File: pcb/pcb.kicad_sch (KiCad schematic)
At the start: 143 parts, among them J1 USB_C_Receptacle_USB2.0_14P, J2 Conn_01x06_Socket, M1 Ezurio BL54L15 (nrf54L15) mod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, SW1 SW_DIP_x01

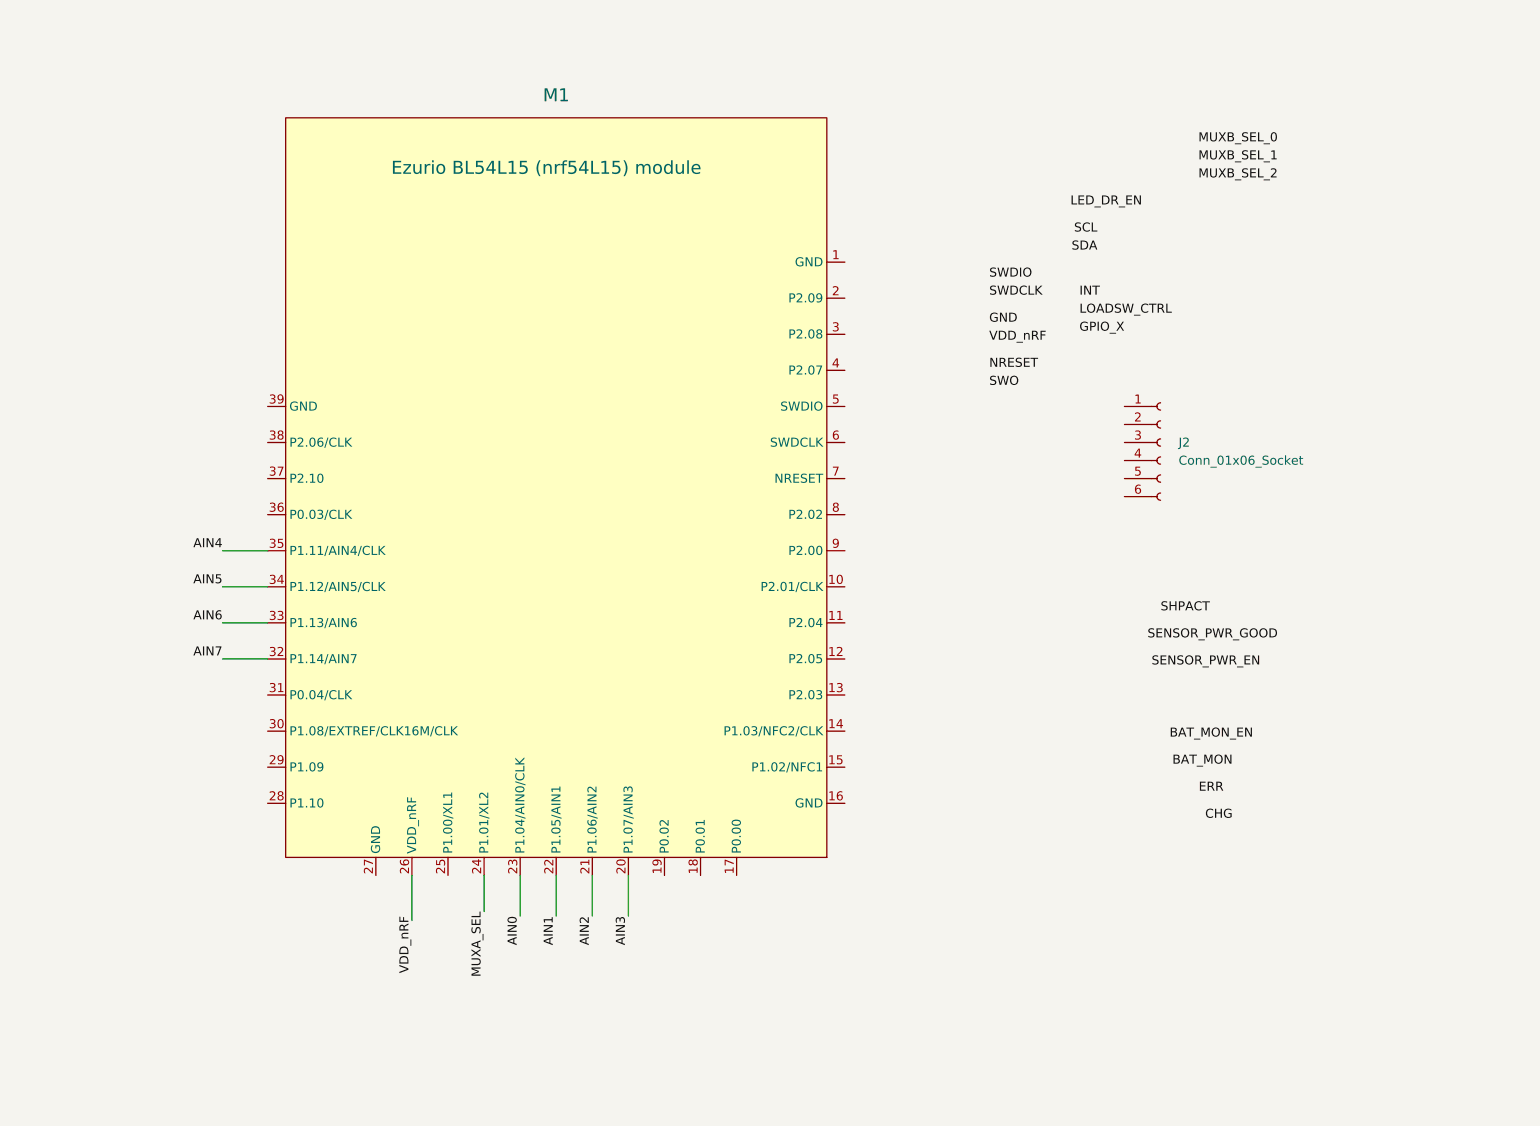
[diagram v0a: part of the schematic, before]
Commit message: M  pcb/pcb.kicad_pcb M  pcb/pcb.kicad_prl M  pcb/pcb.kicad_pro M  pcb/pcb.kicad_sch M  placefp.py A  tmr-footprints/SAMTEC-CLP-105-02-X-D-A-altium.kicad_mod A  tmr-footprints/SAMTEC-CLP-105-02-X-D-A.kicad_mod
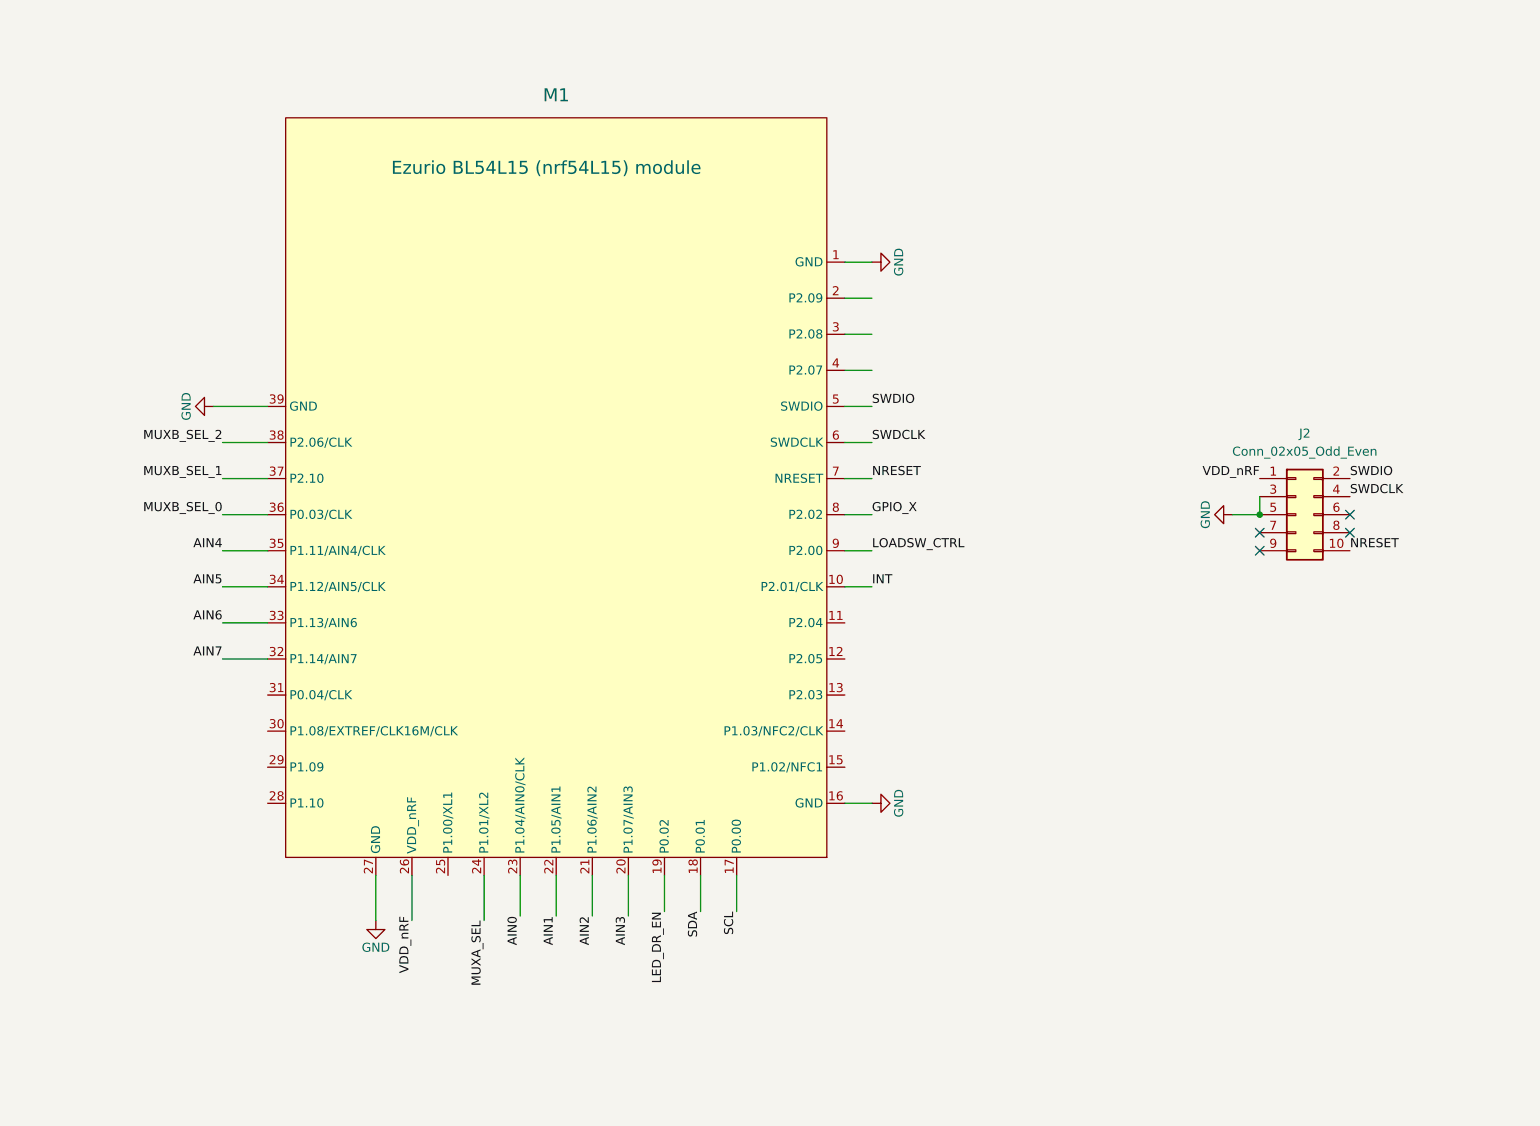
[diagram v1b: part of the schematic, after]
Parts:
- removed J2: Conn_01x06_Socket, symbol Connector:Conn_01x06_Socket
- added J2: Conn_02x05_Odd_Even, tmr-lib:SAMTEC-CLP-105-02-X-D-A, symbol Connector_Generic:Conn_02x05_Odd_Even
- SW1: footprint (none) -> Button_Switch_SMD:SW_SPST_Omron_B3FS-105xP
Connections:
- net GND: now also M1.1 (GND), M1.16 (GND), M1.27 (GND), M1.39 (GND), J2.3 (Pin_3), J2.5 (Pin_5)
- net GPIO_X: now also M1.8 (P2.02)
- net INT: now also M1.10 (P2.01/CLK)
- net LED_DR_EN: now also M1.19 (P0.02)
- net LOADSW_CTRL: now also M1.9 (P2.00)
- net MUXB_SEL_0: now also M1.36 (P0.03/CLK)
- net MUXB_SEL_1: now also M1.37 (P2.10)
- net MUXB_SEL_2: now also M1.38 (P2.06/CLK)
- net NRESET: now also M1.7 (NRESET), J2.10 (Pin_10)
- net SCL: now also M1.17 (P0.00)
- net SDA: now also M1.18 (P0.01)
- net SWDCLK: now also M1.6 (SWDCLK), J2.4 (Pin_4)
- net SWDIO: now also M1.5 (SWDIO), J2.2 (Pin_2)
- net VDDIO: now also J2.1 (Pin_1)
- no-connect marks 9 -> 13

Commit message: M  pcb/pcb.kicad_pcb M  pcb/pcb.kicad_prl M  pcb/pcb.kicad_sch M  placefp.py M  tmr-footprints/Ezurio_BL54L15_Module.kicad_mod
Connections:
- net CS0: now also D24.1 (K), D38.1 (K), D53.1 (K), D9.1 (K); no longer D1.1 (K), D16.1 (K), D30.1 (K), D45.1 (K)
- net CS1: now also D10.1 (K), D25.1 (K), D39.1 (K), D54.1 (K); no longer D17.1 (K), D2.1 (K), D31.1 (K), D46.1 (K)
- net CS10: now also D1.1 (K), D16.1 (K), D30.1 (K), D45.1 (K); no longer D24.1 (K), D38.1 (K), D53.1 (K), D9.1 (K)
- net CS11: now also D17.1 (K), D2.1 (K), D31.1 (K), D46.1 (K); no longer D10.1 (K), D25.1 (K), D39.1 (K), D54.1 (K)
- net CS12: now also D18.1 (K), D3.1 (K), D32.1 (K), D47.1 (K); no longer D11.1 (K), D26.1 (K), D40.1 (K), D55.1 (K)
- net CS13: now also D19.1 (K), D33.1 (K), D4.1 (K), D48.1 (K); no longer D12.1 (K), D27.1 (K), D41.1 (K), D56.1 (K)
- net CS14: now also D20.1 (K), D34.1 (K), D49.1 (K), D5.1 (K); no longer D13.1 (K), D28.1 (K), D42.1 (K), D57.1 (K)
- net CS15: now also D21.1 (K), D35.1 (K), D50.1 (K), D6.1 (K); no longer D14.1 (K), D29.1 (K), D43.1 (K), D58.1 (K)
- net CS16: now also D22.1 (K), D36.1 (K), D51.1 (K), D7.1 (K); no longer D15.1 (K), D44.1 (K), D71.1 (K), D72.1 (K)
- net CS17: now also D23.1 (K), D37.1 (K), D52.1 (K), D8.1 (K); no longer D67.1 (K), D68.1 (K), D69.1 (K), D70.1 (K)
- net CS2: now also D11.1 (K), D26.1 (K), D40.1 (K), D55.1 (K); no longer D18.1 (K), D3.1 (K), D32.1 (K), D47.1 (K)
- net CS3: now also D12.1 (K), D27.1 (K), D41.1 (K), D56.1 (K); no longer D19.1 (K), D33.1 (K), D4.1 (K), D48.1 (K)
- net CS4: now also D13.1 (K), D28.1 (K), D42.1 (K), D57.1 (K); no longer D20.1 (K), D34.1 (K), D49.1 (K), D5.1 (K)
- net CS5: now also D14.1 (K), D29.1 (K), D43.1 (K), D58.1 (K); no longer D21.1 (K), D35.1 (K), D50.1 (K), D6.1 (K)
- net CS6: now also D15.1 (K), D44.1 (K), D71.1 (K), D72.1 (K); no longer D22.1 (K), D36.1 (K), D51.1 (K), D7.1 (K)
- net CS7: now also D67.1 (K), D68.1 (K), D69.1 (K), D70.1 (K); no longer D23.1 (K), D37.1 (K), D52.1 (K), D8.1 (K)
- net CS8: now also D63.1 (K), D64.1 (K), D65.1 (K), D66.1 (K); no longer D59.1 (K), D60.1 (K), D61.1 (K), D62.1 (K)
- net CS9: now also D59.1 (K), D60.1 (K), D61.1 (K), D62.1 (K); no longer D63.1 (K), D64.1 (K), D65.1 (K), D66.1 (K)
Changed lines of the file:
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@@
 	)
 	(label "CS2"
-		(at 396.24 426.72 180)
+		(at 467.36 426.72 180)
 		(effects
 			(font
@@
 	)
 	(label "CS3"
-		(at 405.13 426.72 180)
+		(at 476.25 426.72 180)
 		(effects
 			(font
@@
 	)
 	(label "CS16"
-		(at 502.92 426.72 180)
+		(at 431.8 426.72 180)
 		(effects
 			(font
@@
 		)
 	)
-	(label "CS9"
-		(at 414.02 441.96 180)
-		(effects
-			(font
-				(size 1.27 1.27)
-			)
-			(justify right bottom)
-		)
-	)
 	(label "ANA_70"
 		(at 170.18 294.64 180)
@@
 	)
 	(label "CS1"
-		(at 387.35 426.72 180)
+		(at 458.47 426.72 180)
 		(effects
 			(font
@@
 	)
 	(label "CS6"
-		(at 431.8 426.72 180)
+		(at 502.92 426.72 180)
 		(effects
 			(font
@@
 	)
 	(label "CS12"
-		(at 467.36 426.72 180)
+		(at 396.24 426.72 180)
 		(effects
 			(font
@@
 		)
 	)
+	(label "CS9"
+		(at 378.46 441.96 180)
+		(effects
+			(font
+				(size 1.27 1.27)
+			)
+			(justify right bottom)
+		)
+	)
 	(label "ANA_34"
 		(at 170.18 223.52 180)
@@
 	)
 	(label "CS7"
-		(at 440.69 426.72 180)
+		(at 476.25 441.96 180)
 		(effects
 			(font
@@
 	)
 	(label "CS5"
-		(at 422.91 426.72 180)
+		(at 494.03 426.72 180)
 		(effects
 			(font
@@
 	)
 	(label "CS10"
-		(at 449.58 426.72 180)
+		(at 378.46 426.72 180)
 		(effects
 			(font
@@
 	)
 	(label "CS15"
-		(at 494.03 426.72 180)
+		(at 422.91 426.72 180)
 		(effects
 			(font
@@
 		)
 	)
-	(label "CS17"
-		(at 476.25 441.96 180)
-		(effects
-			(font
-				(size 1.27 1.27)
-			)
-			(justify right bottom)
-		)
-	)
 	(label "ANA_71"
 		(at 204.47 134.62 0)
@@
 		)
 	)
-	(label "CS16"
+	(label "CS6"
 		(at 494.03 441.96 180)
 		(effects
@@
 		)
 	)
-	(label "CS16"
+	(label "CS6"
 		(at 485.14 441.96 180)
 		(effects
@@
 	)
 	(label "CS11"
-		(at 458.47 426.72 180)
+		(at 387.35 426.72 180)
 		(effects
 			(font
@@
 	)
 	(label "CS4"
-		(at 414.02 426.72 180)
+		(at 485.14 426.72 180)
 		(effects
 			(font
@@
 	)
 	(label "CS8"
-		(at 378.46 441.96 180)
+		(at 414.02 441.96 180)
 		(effects
 			(font
@@
 		)
 	)
+	(label "CS17"
+		(at 440.69 426.72 180)
+		(effects
+			(font
+				(size 1.27 1.27)
+			)
+			(justify right bottom)
+		)
+	)
 	(label "ANA_52"
 		(at 213.36 279.4 180)
@@
 	)
 	(label "CS14"
-		(at 485.14 426.72 180)
+		(at 414.02 426.72 180)
 		(effects
 			(font
@@
 	)
 	(label "CS0"
-		(at 378.46 426.72 180)
+		(at 449.58 426.72 180)
 		(effects
 			(font
@@
 	)
 	(label "CS13"
-		(at 476.25 426.72 180)
-		(effects
-			(font
+		(at 405.13 426.72 180)
+		(effects
+			(font

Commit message: M  pcb/pcb.kicad_pcb M  pcb/pcb.kicad_prl M  pcb/pcb.kicad_sch M  pcb/switch.kicad_sch M  placefp.py A  tmr-footprints/Button_Switch_3x4x2.5.kicad_mod A  tmr-footprints/Panasonic_EVPAE.kicad_mod
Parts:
- removed J1: USB_C_Receptacle_USB2.0_14P, symbol Connector:USB_C_Receptacle_USB2.0_14P
- removed JLC1: JLC_Order_Num, tmr-lib:JLC_Order_Num, symbol giri:JLC_Order_Num
- added JLC1: JLC_Order_Num, tmr-lib:JLC_Order_Num, symbol tmr-lib:JLC_Order_Num
- added JTAG2: Conn_02x05_Odd_Even, Connector:Tag-Connect_TC2050-IDC-FP_2x05_P1.27mm_Vertical, symbol Connector_Generic:Conn_02x05_Odd_Even
- BAT1: value Battery_Pack_PS5 -> ~; footprint Connector_JST:JST_EH_S3B-EH_1x03_P2.50mm_Horizontal -> Connector_JST:JST_SH_BM03B-SRSS-TB_1x03-1MP_P1.00mm_Vertical
- SW1: footprint Button_Switch_SMD:SW_SPST_Omron_B3FS-105xP -> tmr-lib:Button_Switch_3x4x2.5
- renumbered C6 to C1, C15 to C10, C16 to C11, C17 to C12, C18 to C13, C5 to C14, C7 to C15, C20 to C16, C21 to C17, C22 to C18, C23 to C19, C8 to C2, C24 to C20, C12 to C21, C13 to C22, C14 to C23, C27 to C24, C28 to C25, C29 to C26, C30 to C27, C19 to C28, C25 to C29, C9 to C3, C26 to C30, C10 to C4, C11 to C5, C1 to C6, C2 to C7, C3 to C8, C4 to C9, J2 to JTAG1
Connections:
- net VCC_tmr is gone; now on net VCCS: C23.1, PMIC1.29 (LSOUT1/VOUTLDO1)
- net GND: now also JTAG2.3 (Pin_3), JTAG2.5 (Pin_5)
- net NRESET: now also JTAG2.10 (Pin_10)
- net SWDCLK: now also JTAG2.4 (Pin_4)
- net SWDIO: now also JTAG2.2 (Pin_2)
- net VCCS: no longer C22.1, L2.1, PMIC1.28 (LSIN1/VINLDO1), PMIC1.32 (VOUT2)
- net VDDIO: now also JTAG2.1 (Pin_1)
- new net VOUT2: C22.1, L2.1, PMIC1.28 (LSIN1/VINLDO1), PMIC1.32 (VOUT2)
- no-connect marks 13 -> 26
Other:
- moved on the sheet: BAT1, C14, C15, C21, C22, C23, C28, C29, C30, C31, C32, C6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

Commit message: M  pcb/pcb.kicad_pcb M  pcb/pcb.kicad_sch A  tmr-footprints/MountingHole_2.2mm_M2_ISO7380_Pad_TopBottom.kicad_mod
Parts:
- Hs1, Hs10, Hs11, Hs12, Hs2, Hs3, Hs4, Hs5, Hs6, Hs7, Hs8, Hs9: footprint MountingHole:MountingHole_2.2mm_M2_ISO7380_Pad_TopBottom -> tmr-lib:MountingHole_2.2mm_M2_ISO7380_Pad_TopBottom
- JTAG2: footprint Connector:Tag-Connect_TC2050-IDC-FP_2x05_P1.27mm_Vertical -> Connector:Tag-Connect_TC2050-IDC-NL_2x05_P1.27mm_Vertical
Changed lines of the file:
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@@
 			)
 		)
-		(property "Footprint" "MountingHole:MountingHole_2.2mm_M2_ISO7380_Pad_TopBottom"
+		(property "Footprint" "tmr-lib:MountingHole_2.2mm_M2_ISO7380_Pad_TopBottom"
 			(at 359.41 364.49 0)
 			(effects
@@
 			)
 		)
-		(property "Footprint" "MountingHole:MountingHole_2.2mm_M2_ISO7380_Pad_TopBottom"
+		(property "Footprint" "tmr-lib:MountingHole_2.2mm_M2_ISO7380_Pad_TopBottom"
 			(at 359.41 372.11 0)
 			(effects
@@
 			)
 		)
-		(property "Footprint" "Connector:Tag-Connect_TC2050-IDC-FP_2x05_P1.27mm_Vertical"
+		(property "Footprint" "Connector:Tag-Connect_TC2050-IDC-NL_2x05_P1.27mm_Vertical"
 			(at 492.76 133.35 0)
 			(effects
@@
 			)
 		)
-		(property "Footprint" "MountingHole:MountingHole_2.2mm_M2_ISO7380_Pad_TopBottom"
+		(property "Footprint" "tmr-lib:MountingHole_2.2mm_M2_ISO7380_Pad_TopBottom"
 			(at 384.81 364.49 0)
 			(effects
@@
 			)
 		)
-		(property "Footprint" "MountingHole:MountingHole_2.2mm_M2_ISO7380_Pad_TopBottom"
+		(property "Footprint" "tmr-lib:MountingHole_2.2mm_M2_ISO7380_Pad_TopBottom"
 			(at 372.11 364.49 0)
 			(effects
@@
 			)
 		)
-		(property "Footprint" "MountingHole:MountingHole_2.2mm_M2_ISO7380_Pad_TopBottom"
+		(property "Footprint" "tmr-lib:MountingHole_2.2mm_M2_ISO7380_Pad_TopBottom"
 			(at 397.51 372.11 0)
 			(effects
@@
 			)
 		)
-		(property "Footprint" "MountingHole:MountingHole_2.2mm_M2_ISO7380_Pad_TopBottom"
+		(property "Footprint" "tmr-lib:MountingHole_2.2mm_M2_ISO7380_Pad_TopBottom"
 			(at 372.11 372.11 0)
 			(effects
@@
 			)
 		)
-		(property "Footprint" "MountingHole:MountingHole_2.2mm_M2_ISO7380_Pad_TopBottom"
+		(property "Footprint" "tmr-lib:MountingHole_2.2mm_M2_ISO7380_Pad_TopBottom"
 			(at 359.41 379.73 0)
 			(effects
@@
 			)
 		)
-		(property "Footprint" "MountingHole:MountingHole_2.2mm_M2_ISO7380_Pad_TopBottom"
+		(property "Footprint" "tmr-lib:MountingHole_2.2mm_M2_ISO7380_Pad_TopBottom"
 			(at 397.51 379.73 0)
 			(effects
@@
 			)
 		)
-		(property "Footprint" "MountingHole:MountingHole_2.2mm_M2_ISO7380_Pad_TopBottom"
+		(property "Footprint" "tmr-lib:MountingHole_2.2mm_M2_ISO7380_Pad_TopBottom"
 			(at 384.81 372.11 0)
 			(effects
@@
 			)
 		)
-		(property "Footprint" "MountingHole:MountingHole_2.2mm_M2_ISO7380_Pad_TopBottom"
+		(property "Footprint" "tmr-lib:MountingHole_2.2mm_M2_ISO7380_Pad_TopBottom"
 			(at 372.11 379.73 0)
 			(effects
@@
 			)
 		)
-		(property "Footprint" "MountingHole:MountingHole_2.2mm_M2_ISO7380_Pad_TopBottom"
+		(property "Footprint" "tmr-lib:MountingHole_2.2mm_M2_ISO7380_Pad_TopBottom"
 			(at 384.81 379.73 0)
 			(effects
@@
 			)
 		)
-		(property "Footprint" "MountingHole:MountingHole_2.2mm_M2_ISO7380_Pad_TopBottom"
+		(property "Footprint" "tmr-lib:MountingHole_2.2mm_M2_ISO7380_Pad_TopBottom"
 			(at 397.51 364.49 0)
 			(effects

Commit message: M  pcb/pcb.kicad_pcb M  pcb/pcb.kicad_prl M  pcb/pcb.kicad_pro M  pcb/pcb.kicad_sch M  placefp.py M  tmr-footprints/MountingHole_2.2mm_M2_ISO7380_Pad_TopBottom.kicad_mod M  tracks.py
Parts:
- BAT1: footprint Connector_JST:JST_SH_BM03B-SRSS-TB_1x03-1MP_P1.00mm_Vertical -> Connector_JST:JST_SH_SM03B-SRSS-TB_1x03-1MP_P1.00mm_Horizontal
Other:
- moved on the sheet: C29, C30, C31, C32, D1, D10, D11, D12, D13, D14, D15, D16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

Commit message: M  pcb/pcb.kicad_pcb M  pcb/pcb.kicad_prl M  pcb/pcb.kicad_sch D  tmr-footprints/MountingHole_2.2mm_M2_ISO7380_Pad_TopBottom.kicad_mod
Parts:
- Hs1, Hs10, Hs11, Hs12, Hs2, Hs3, Hs4, Hs5, Hs6, Hs7, Hs8, Hs9: footprint tmr-lib:MountingHole_2.2mm_M2_ISO7380_Pad_TopBottom -> MountingHole:MountingHole_2.2mm_M2_ISO7380_Pad_TopBottom
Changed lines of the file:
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@@
 			)
 		)
-		(property "Footprint" "tmr-lib:MountingHole_2.2mm_M2_ISO7380_Pad_TopBottom"
+		(property "Footprint" "MountingHole:MountingHole_2.2mm_M2_ISO7380_Pad_TopBottom"
 			(at 359.41 364.49 0)
 			(effects
@@
 			)
 		)
-		(property "Footprint" "tmr-lib:MountingHole_2.2mm_M2_ISO7380_Pad_TopBottom"
+		(property "Footprint" "MountingHole:MountingHole_2.2mm_M2_ISO7380_Pad_TopBottom"
 			(at 359.41 372.11 0)
 			(effects
@@
 			)
 		)
-		(property "Footprint" "tmr-lib:MountingHole_2.2mm_M2_ISO7380_Pad_TopBottom"
+		(property "Footprint" "MountingHole:MountingHole_2.2mm_M2_ISO7380_Pad_TopBottom"
 			(at 384.81 364.49 0)
 			(effects
@@
 			)
 		)
-		(property "Footprint" "tmr-lib:MountingHole_2.2mm_M2_ISO7380_Pad_TopBottom"
+		(property "Footprint" "MountingHole:MountingHole_2.2mm_M2_ISO7380_Pad_TopBottom"
 			(at 372.11 364.49 0)
 			(effects
@@
 			)
 		)
-		(property "Footprint" "tmr-lib:MountingHole_2.2mm_M2_ISO7380_Pad_TopBottom"
+		(property "Footprint" "MountingHole:MountingHole_2.2mm_M2_ISO7380_Pad_TopBottom"
 			(at 397.51 372.11 0)
 			(effects
@@
 			)
 		)
-		(property "Footprint" "tmr-lib:MountingHole_2.2mm_M2_ISO7380_Pad_TopBottom"
+		(property "Footprint" "MountingHole:MountingHole_2.2mm_M2_ISO7380_Pad_TopBottom"
 			(at 372.11 372.11 0)
 			(effects
@@
 			)
 		)
-		(property "Footprint" "tmr-lib:MountingHole_2.2mm_M2_ISO7380_Pad_TopBottom"
+		(property "Footprint" "MountingHole:MountingHole_2.2mm_M2_ISO7380_Pad_TopBottom"
 			(at 359.41 379.73 0)
 			(effects
@@
 			)
 		)
-		(property "Footprint" "tmr-lib:MountingHole_2.2mm_M2_ISO7380_Pad_TopBottom"
+		(property "Footprint" "MountingHole:MountingHole_2.2mm_M2_ISO7380_Pad_TopBottom"
 			(at 397.51 379.73 0)
 			(effects
@@
 			)
 		)
-		(property "Footprint" "tmr-lib:MountingHole_2.2mm_M2_ISO7380_Pad_TopBottom"
+		(property "Footprint" "MountingHole:MountingHole_2.2mm_M2_ISO7380_Pad_TopBottom"
 			(at 384.81 372.11 0)
 			(effects
@@
 			)
 		)
-		(property "Footprint" "tmr-lib:MountingHole_2.2mm_M2_ISO7380_Pad_TopBottom"
+		(property "Footprint" "MountingHole:MountingHole_2.2mm_M2_ISO7380_Pad_TopBottom"
 			(at 372.11 379.73 0)
 			(effects
@@
 			)
 		)
-		(property "Footprint" "tmr-lib:MountingHole_2.2mm_M2_ISO7380_Pad_TopBottom"
+		(property "Footprint" "MountingHole:MountingHole_2.2mm_M2_ISO7380_Pad_TopBottom"
 			(at 384.81 379.73 0)
 			(effects
@@
 			)
 		)
-		(property "Footprint" "tmr-lib:MountingHole_2.2mm_M2_ISO7380_Pad_TopBottom"
+		(property "Footprint" "MountingHole:MountingHole_2.2mm_M2_ISO7380_Pad_TopBottom"
 			(at 397.51 364.49 0)
 			(effects
